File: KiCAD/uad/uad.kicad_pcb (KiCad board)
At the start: 2 copper layers, 50 x 50 mm, 29 parts

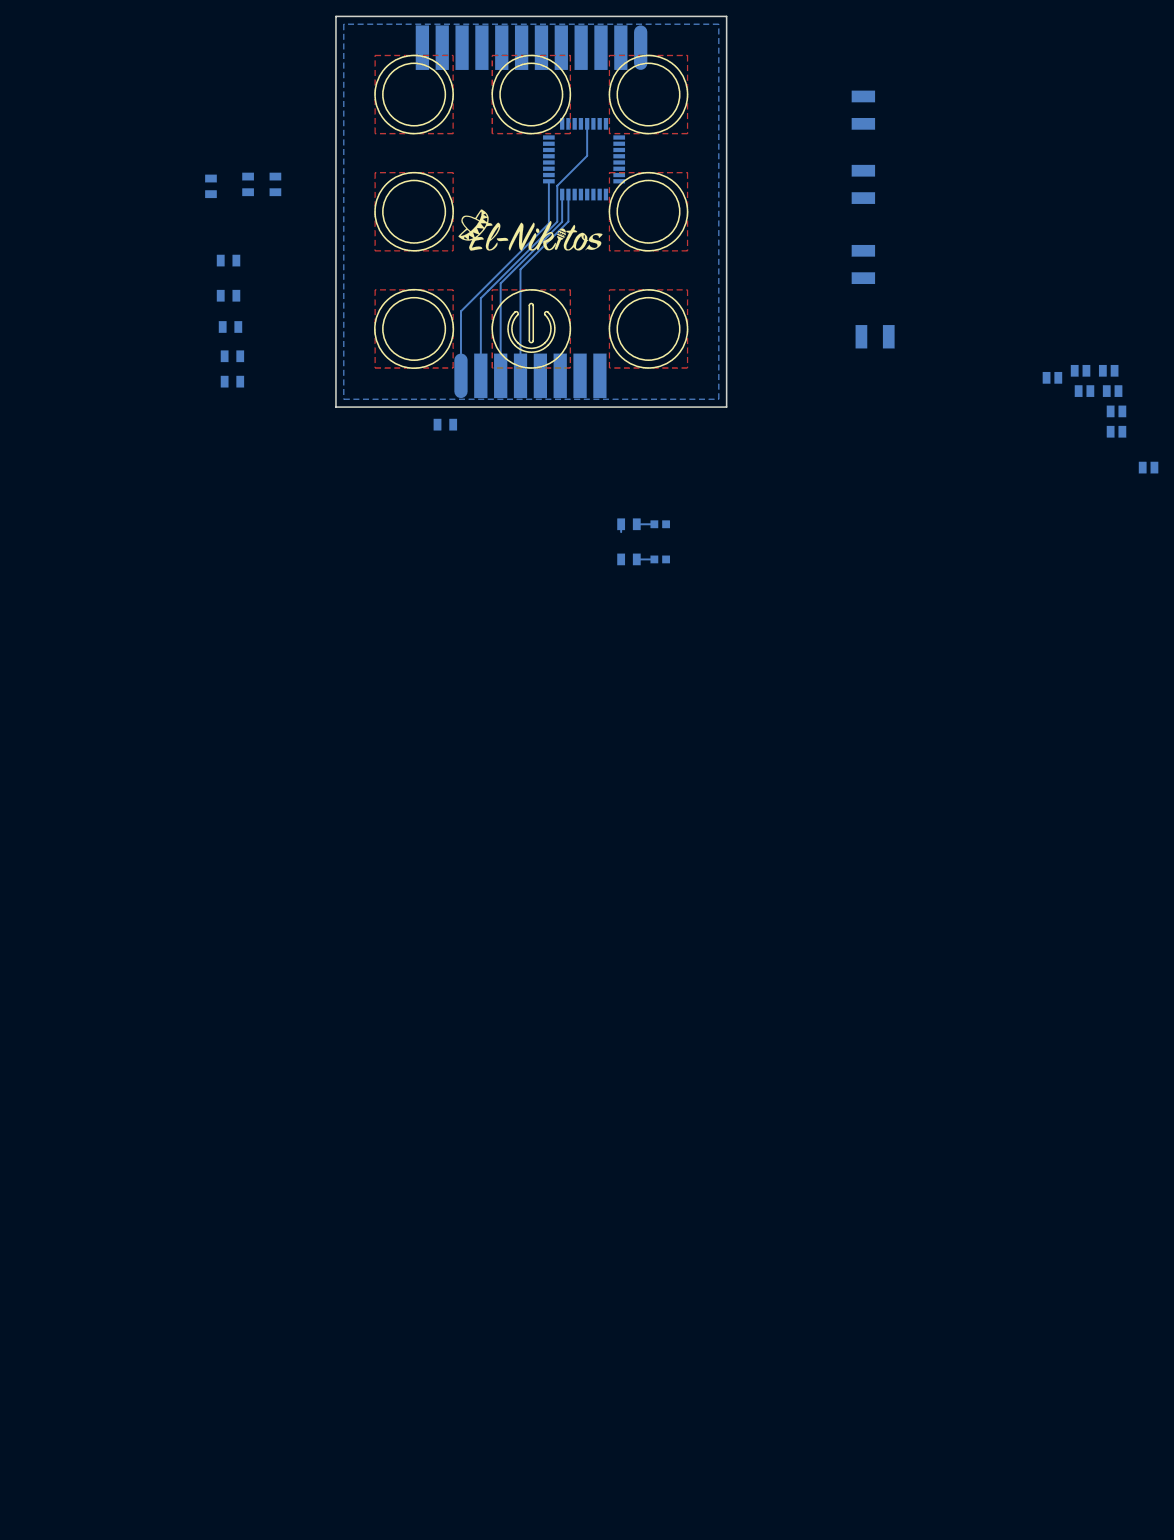
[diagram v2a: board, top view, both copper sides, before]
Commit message: проект разбит на листы, лицевая панель расставлена, но не разведена
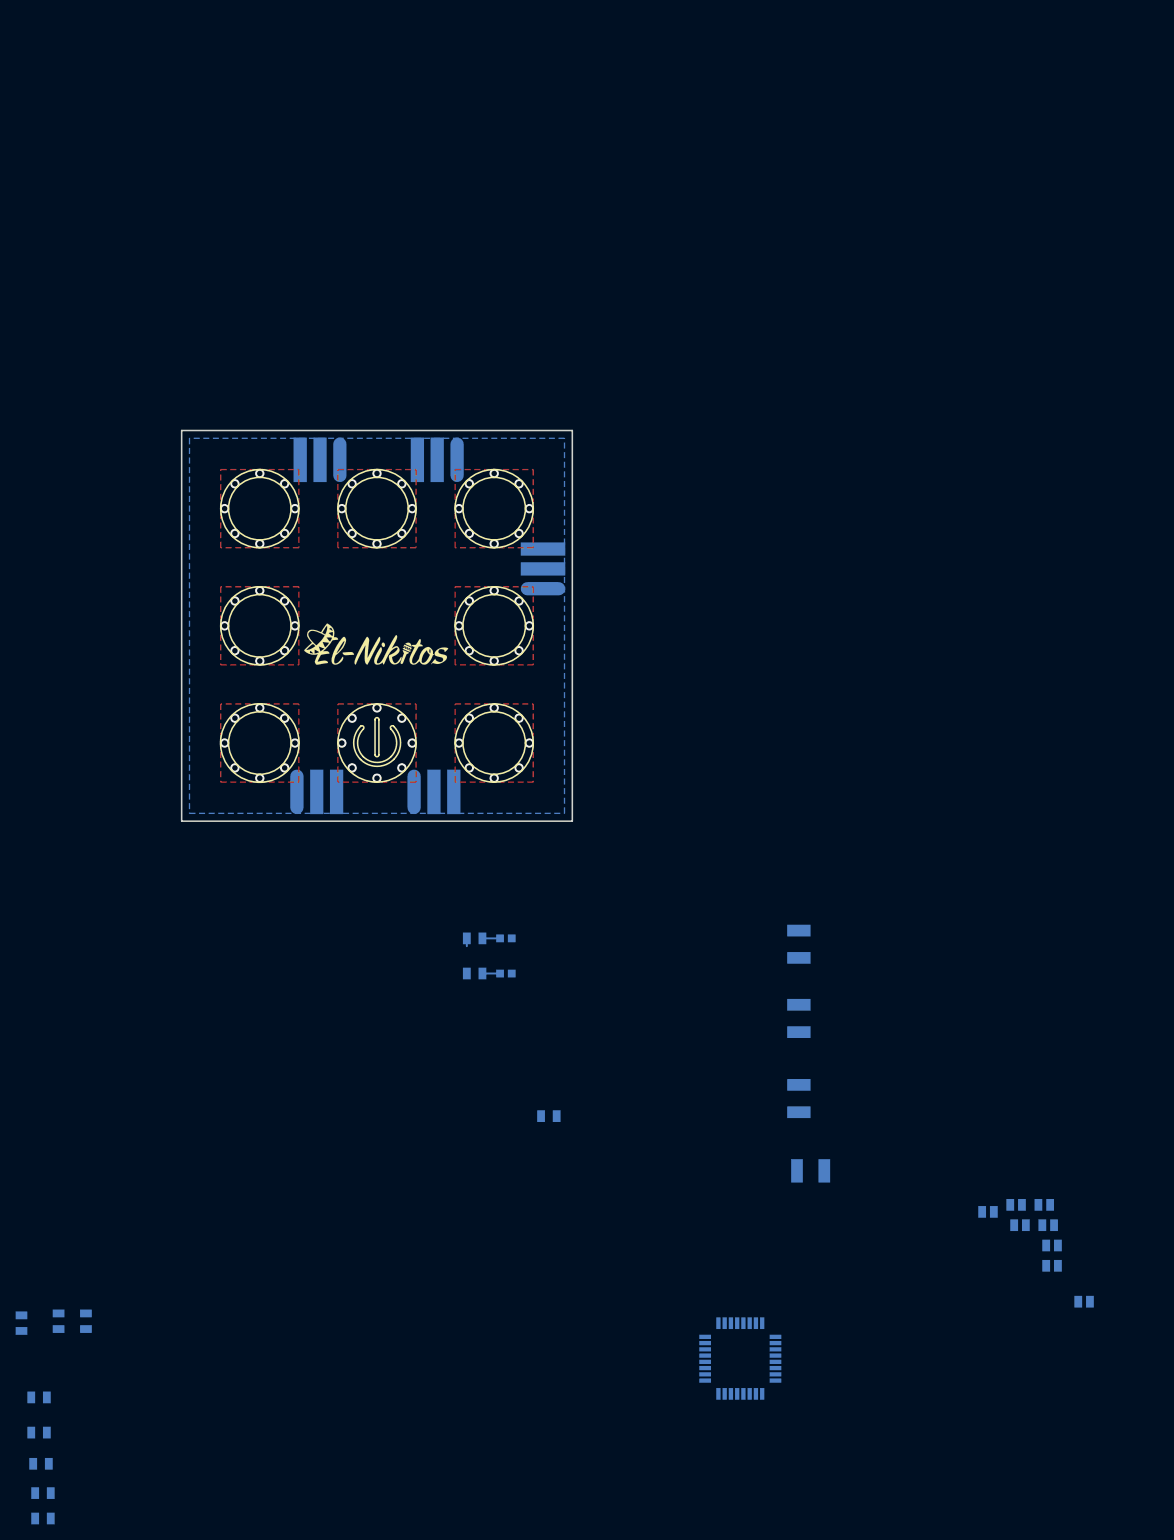
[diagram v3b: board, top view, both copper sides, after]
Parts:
- added XP3: Вилка_PLS3, N_X:Вилка_PLS3_угловая_вертикальная, B.Cu at (90.5, 99.8)
- added XP4: Вилка_PLS3, N_X:Вилка_PLS3_угловая_вертикальная, B.Cu at (105.5, 99.8)
- added XP5: Вилка_PLS3, N_X:Вилка_PLS3_угловая_вертикальная, B.Cu at (118.5, 118.2)
- XP1: value Вилка_PLS8 -> Вилка_PLS3; footprint N_X:Вилка_PLS8_угловая_вертикальная -> N_X:Вилка_PLS3_угловая_вертикальная
- XP2: value Вилка_PLS12 -> Вилка_PLS3; footprint N_X:Вилка_PLS12_угловая_вертикальная -> N_X:Вилка_PLS3_угловая_вертикальная
- moved DD1 154.8 mm to (146.0, 214.0)
- moved R1 147.5 mm to (54.5, 211.0)
- moved R2 147.5 mm to (49.8, 211.2)
- moved R3 147.5 mm to (58.0, 211.0)
- moved R4 147.5 mm to (51.0, 221.8)
- moved R5 147.5 mm to (51.0, 226.2)
- moved R6 147.5 mm to (51.2, 230.2)
- moved R7 147.5 mm to (51.5, 234.0)
- moved R8 147.5 mm to (51.5, 237.2)
- moved C8 107.1 mm to (172.7, 198.0)
- moved C1 107.1 mm to (185.0, 209.5)
- moved C10 107.1 mm to (149.2, 162.0)
- moved C11 107.1 mm to (149.2, 171.5)
- moved C12 107.1 mm to (149.0, 192.8)
- moved C2 107.1 mm to (179.9, 197.1)
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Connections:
- net BUT_0_CUP renamed /uad_sensor/BUT_1_CUP
- net BUT_1_CUP renamed /uad_sensor/BUT_2_CUP
- net BUT_2_CUP renamed /uad_sensor/BUT_3_CUP
- net BUT_3_CUP renamed /uad_sensor/BUT_4_CUP
- net BUT_4_CUP renamed /uad_sensor/BUT_5_CUP
- net BUT_5_CUP renamed /uad_sensor/BUT_6_CUP
- net BUT_6_CUP renamed /uad_sensor/BUT_7_CUP
- net BUT_7_CUP renamed /uad_sensor/BUT_8_CUP
- C1 pad 1: GND -> /uad_sensor/GND
- C2 pad 1: GND -> /uad_sensor/GND
- C3 pad 1: GND -> /uad_sensor/GND
- C4 pad 1: GND -> /uad_sensor/GND
- C5 pad 1: GND -> /uad_sensor/GND
- C6 pad 1: GND -> /uad_sensor/GND
- C7 pad 1: GND -> /uad_sensor/GND
- C8 pad 1: GND -> /uad_sensor/GND
- R1 pad 1: BUT_COM_OUT -> /uad_sensor/BUT_COM_OUT
- R2 pad 1: BUT_COM_OUT -> /uad_sensor/BUT_COM_OUT
- R3 pad 1: BUT_COM_OUT -> /uad_sensor/BUT_COM_OUT
- R4 pad 1: BUT_COM_OUT -> /uad_sensor/BUT_COM_OUT
- R5 pad 1: BUT_COM_OUT -> /uad_sensor/BUT_COM_OUT
- R6 pad 1: BUT_COM_OUT -> /uad_sensor/BUT_COM_OUT
- R7 pad 1: BUT_COM_OUT -> /uad_sensor/BUT_COM_OUT
- R8 pad 1: BUT_COM_OUT -> /uad_sensor/BUT_COM_OUT
- XP1 pad 1: SCK -> /uad_sensor/BUT_COM_OUT
- XP1 pad 2: RES -> /uad_sensor/GND
- XP1 pad 3: MISO -> /uad_sensor/GND
- XP2 pad 1: D_Out_1 -> /uad_sensor/GND
- XP2 pad 2: D_Out_2 -> /uad_sensor/GND
- XP2 pad 3: D_Out_3 -> /uad_sensor/BUT_COM_OUT
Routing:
- net RES: track 39.9 -> 0.00 mm
- net SCK: track 31.6 -> 0.00 mm
- net MISO: track 28.5 -> 0.00 mm
- net MOSI: track 27.7 -> 0.00 mm
- net VCC: vias 0 -> 1
- net TX: vias 0 -> 2
- net D_Out_6: vias 0 -> 1
- net BUT_6_CUP: vias 0 -> 7
- net /uad_sensor/GND: vias 0 -> 2
- net /uad_sensor/BUT_8_CUP: vias 0 -> 7
- net /uad_sensor/BUT_7_CUP: vias 0 -> 4
- net /uad_sensor/BUT_5_CUP: vias 0 -> 7
- net /uad_sensor/BUT_4_CUP: vias 0 -> 9
- net /uad_sensor/BUT_3_CUP: vias 0 -> 9
- net /uad_sensor/BUT_2_CUP: vias 0 -> 8
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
